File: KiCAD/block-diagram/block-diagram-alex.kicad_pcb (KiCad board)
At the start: 2 copper layers, 12 parts, among them Q3 NMOS, Q4 NMOS, U1 74LS02, U2 74LS02, U3 74LS11, U6 LMC555xM

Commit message: trying to fix issues
Issues with merging are preventing me to pull origin
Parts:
- removed U2: 74LS02, Package_SO:SOIC-14_3.9x8.7mm_P1.27mm
- moved U3 104.8 mm to (151.8, 90.4)
- moved R1 103.7 mm to (156.0, 97.1)
- moved Q4 102.6 mm to (158.5, 92.2)
- moved R3 101.8 mm to (156.0, 103.7)
- moved R4 100.4 mm to (156.0, 107.0)
- moved C3 96.4 mm to (150.4, 97.2)
- moved Q3 95.3 mm to (158.5, 87.5)
- moved R2 95.2 mm to (156.0, 100.4)
- moved U6 91.5 mm to (143.4, 98.8)
- moved C4 86.4 mm to (150.4, 100.5)
- moved U1 63.3 mm to (143.4, 90.4)
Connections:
- U1 pad 10: unconnected-(U1-Pad10) -> Net-(U1-Pad10)
- U1 pad 8: unconnected-(U1-Pad8) -> Net-(R3-Pad2)
- U1 pad 9: unconnected-(U1-Pad9) -> Net-(SW4-B)
- U3 pad 13: Net-(U2-Pad1) -> Net-(U1-Pad10)

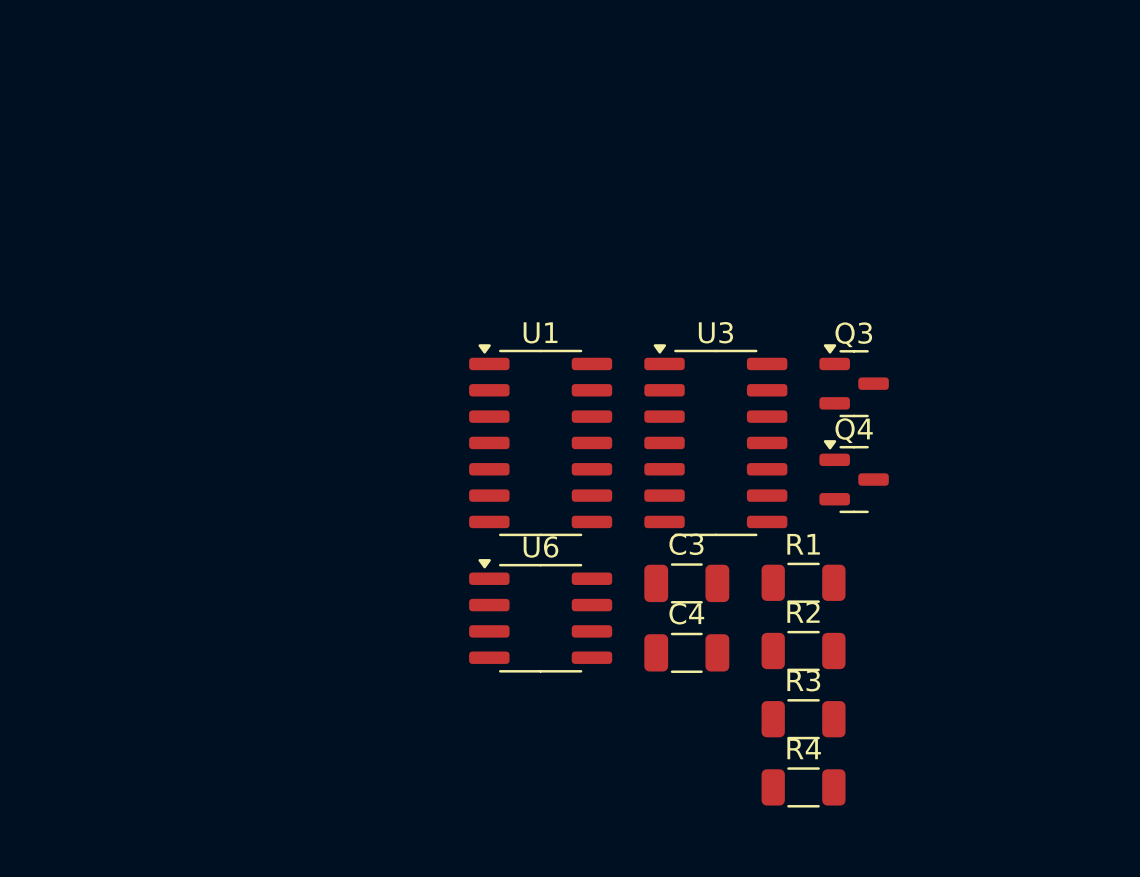
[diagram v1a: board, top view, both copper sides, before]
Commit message: PCB layout updates
I updated the PCB with the components added to the schematic. I dimensioned a rectangle around the board that is 2x1.5 in and placed the 8 pin connecters with respect to the corners of the rectangle. I added the relevant dimensions. Board layout based on our discussion Friday. I remember we were having some discussion on the 4 connectors in each corner of the board, those have not been added yet.
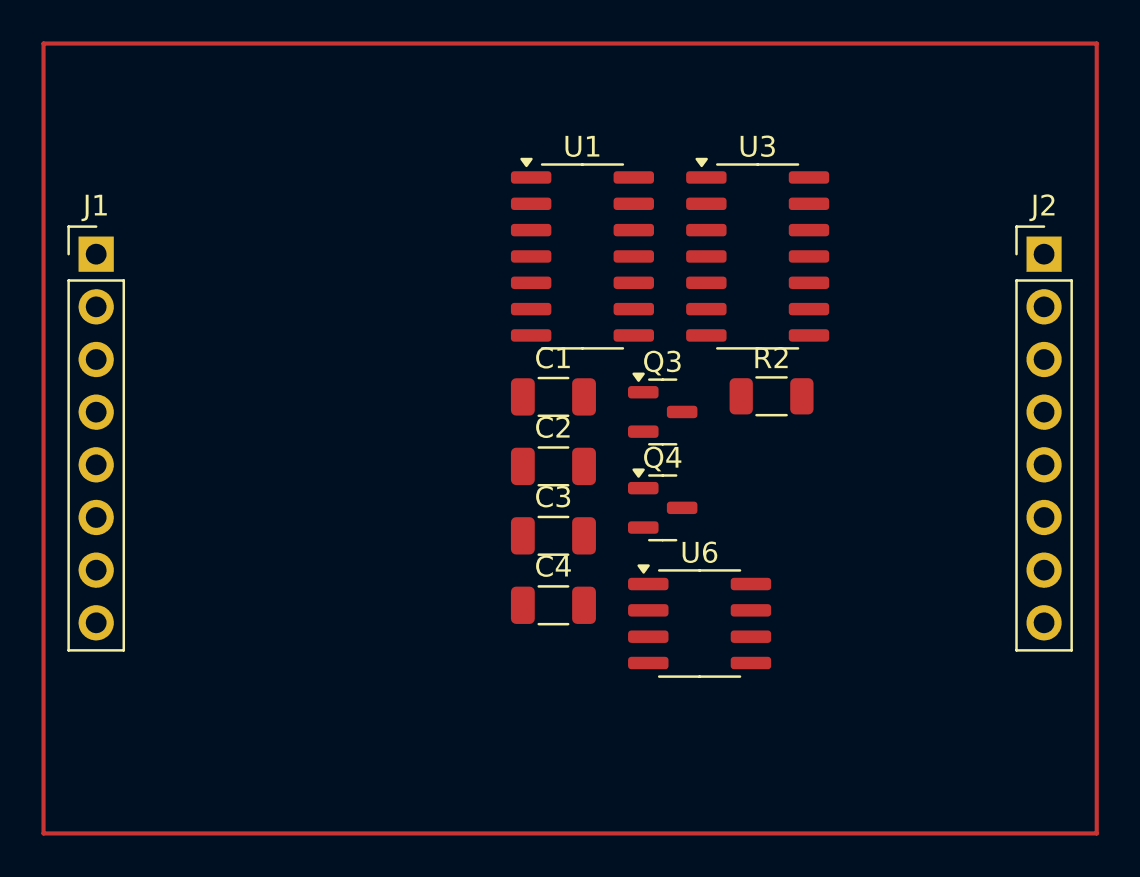
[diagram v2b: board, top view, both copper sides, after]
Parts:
- removed R1, R3, R4: R_US, Resistor_SMD:R_1206_3216Metric
- added C1: C_Small, Capacitor_SMD:C_1206_3216Metric, F.Cu at (144.0, 88.2)
- added C2: C_Small, Capacitor_SMD:C_1206_3216Metric, F.Cu at (144.0, 91.5)
- added J1: Conn_01x08, Connector_PinHeader_2.54mm:PinHeader_1x08_P2.54mm_Vertical, F.Cu at (121.9, 81.3)
- added J2: Conn_01x08, Connector_PinHeader_2.54mm:PinHeader_1x08_P2.54mm_Vertical, F.Cu at (167.6, 81.3)
- moved R2 12.4 mm to (154.5, 88.1)
- moved Q3 9.33 mm to (149.2, 88.9)
- moved Q4 9.33 mm to (149.2, 93.5)
- moved U1 9.22 mm to (145.4, 81.4)
- moved U3 9.22 mm to (153.8, 81.4)
- moved U6 7.67 mm to (151.0, 99.1)
- moved C3 6.83 mm to (144.0, 94.9)
- moved C4 6.83 mm to (144.0, 98.2)
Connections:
- Q4 pad 2: Watchdog_PD_output -> Net-(J1-Pin_3)
- U1 pad 11: unconnected-(U1-Pad11) -> GND
- U1 pad 12: unconnected-(U1-Pad12) -> GND
- U1 pad 14: unconnected-(U1E-VCC-Pad14) -> +5V
- U1 pad 3: Laser_current_high -> Net-(J1-Pin_2)
- U1 pad 7: unconnected-(U1E-GND-Pad7) -> GND
- U3 pad 10: unconnected-(U3-Pad10) -> GND
- U3 pad 11: unconnected-(U3-Pad11) -> GND
- U3 pad 12: LASER_ENA -> Net-(J2-Pin_1)
- U3 pad 14: unconnected-(U3D-VCC-Pad14) -> +5V
- U3 pad 2: Enable_In -> Net-(J1-Pin_4)
- U3 pad 3: unconnected-(U3-Pad3) -> GND
- U3 pad 4: unconnected-(U3-Pad4) -> GND
- U3 pad 5: unconnected-(U3-Pad5) -> GND
- U3 pad 7: unconnected-(U3D-GND-Pad7) -> GND
- U3 pad 9: unconnected-(U3-Pad9) -> GND
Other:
- copper layers 2 -> 4

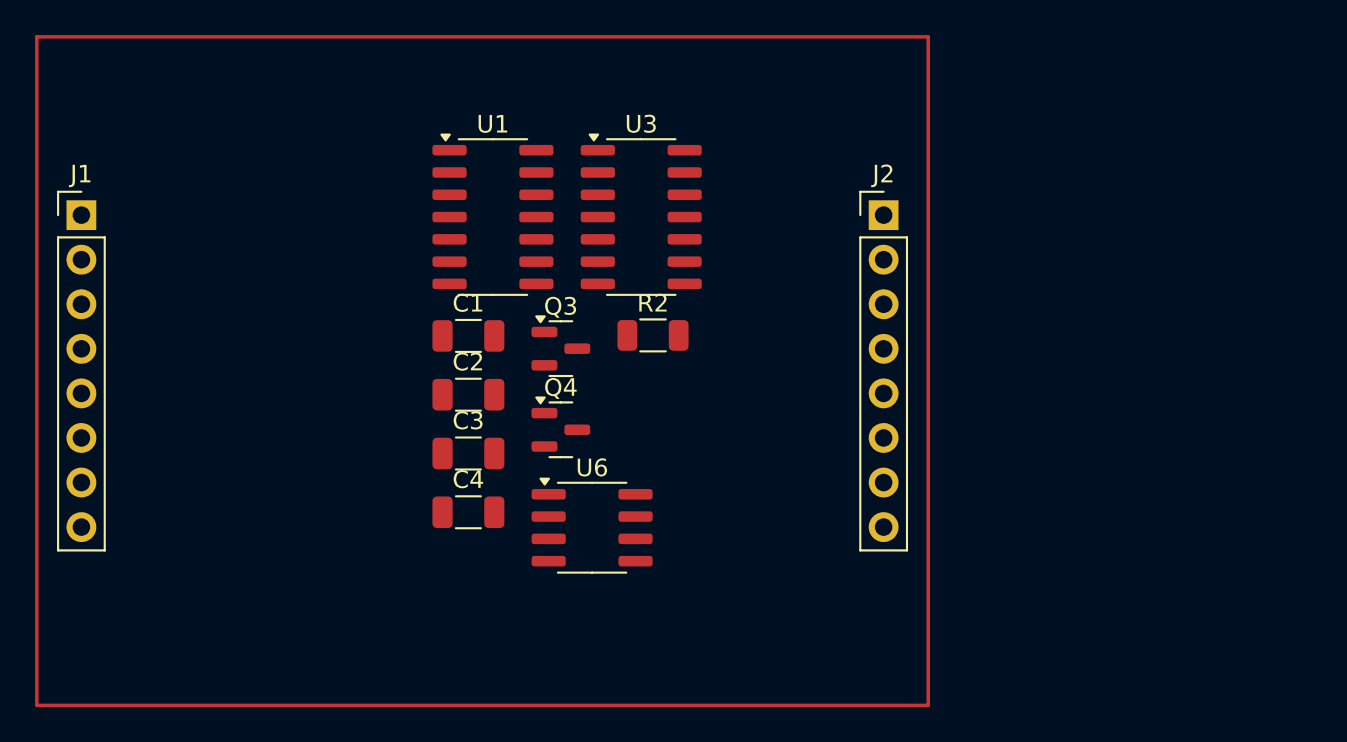
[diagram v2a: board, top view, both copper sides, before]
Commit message: tentative placement, add test points and LEDs
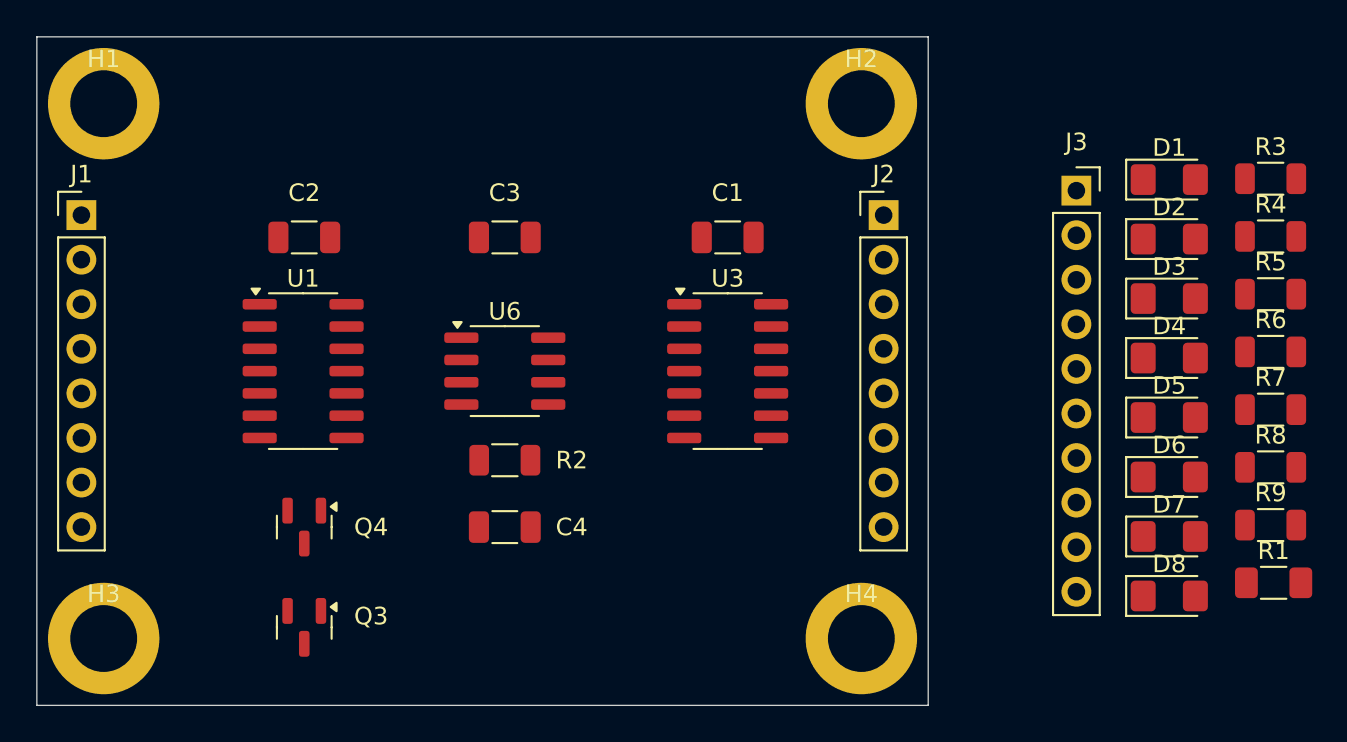
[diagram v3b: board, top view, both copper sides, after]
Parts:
- added D1: LED, LED_SMD:LED_1206_3216Metric_Pad1.42x1.75mm_HandSolder, F.Cu at (183.9, 79.3)
- added D2: LED, LED_SMD:LED_1206_3216Metric_Pad1.42x1.75mm_HandSolder, F.Cu at (183.9, 82.6)
- added D3: LED, LED_SMD:LED_1206_3216Metric_Pad1.42x1.75mm_HandSolder, F.Cu at (183.9, 86.0)
- added D4: LED, LED_SMD:LED_1206_3216Metric_Pad1.42x1.75mm_HandSolder, F.Cu at (183.9, 89.4)
- added D5: LED, LED_SMD:LED_1206_3216Metric_Pad1.42x1.75mm_HandSolder, F.Cu at (183.9, 92.8)
- added D6: LED, LED_SMD:LED_1206_3216Metric_Pad1.42x1.75mm_HandSolder, F.Cu at (183.9, 96.2)
- added D7: LED, LED_SMD:LED_1206_3216Metric_Pad1.42x1.75mm_HandSolder, F.Cu at (183.9, 99.6)
- added D8: LED, LED_SMD:LED_1206_3216Metric_Pad1.42x1.75mm_HandSolder, F.Cu at (183.9, 103.0)
- added H1: MountingHole_Pad, my_mtg_hole:hole_250_150, F.Cu at (123.2, 74.9)
- added H2: MountingHole_Pad, my_mtg_hole:hole_250_150, F.Cu at (166.4, 74.9)
- added H3: MountingHole_Pad, my_mtg_hole:hole_250_150, F.Cu at (123.2, 105.4)
- added H4: MountingHole_Pad, my_mtg_hole:hole_250_150, F.Cu at (166.4, 105.4)
- added J3: Conn_01x10, Connector_PinSocket_2.54mm:PinSocket_1x10_P2.54mm_Vertical, F.Cu at (178.6, 79.9)
- added R1: 470, Resistor_SMD:R_1206_3216Metric_Pad1.30x1.75mm_HandSolder, F.Cu at (189.9, 102.2)
- added R3: 470, Resistor_SMD:R_1206_3216Metric, F.Cu at (189.7, 79.2)
- added R4: 470, Resistor_SMD:R_1206_3216Metric, F.Cu at (189.7, 82.5)
- added R5: 470, Resistor_SMD:R_1206_3216Metric, F.Cu at (189.7, 85.8)
- added R6: 470, Resistor_SMD:R_1206_3216Metric, F.Cu at (189.7, 89.1)
- added R7: 470, Resistor_SMD:R_1206_3216Metric, F.Cu at (189.7, 92.4)
- added R8: 470, Resistor_SMD:R_1206_3216Metric, F.Cu at (189.7, 95.7)
- added R9: 470, Resistor_SMD:R_1206_3216Metric, F.Cu at (189.7, 98.9)
- moved Q3 21.6 mm to (134.6, 104.8), turned to -90 degrees
- moved C1 15.8 mm to (158.8, 82.5), turned to 180 degrees
- moved Q4 15.6 mm to (134.6, 99.1), turned to -90 degrees
- moved U1 13.9 mm to (134.6, 90.2)
- moved C2 13.0 mm to (134.6, 82.5), turned to 180 degrees
- moved C3 12.5 mm to (146.1, 82.5), turned to 180 degrees
- moved R2 11.0 mm to (146.1, 95.2)
- moved U6 10.2 mm to (146.1, 90.2)
- moved U3 10.1 mm to (158.8, 90.2)
- moved C4 2.24 mm to (146.1, 99.1), turned to 180 degrees
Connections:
- net Net-(J1-Pin_1) renamed /OVERRIDE
- net Net-(J1-Pin_2) renamed /LC_HIGH
- net Net-(J1-Pin_3) renamed /WD_PHOTODIODE
- net Net-(J1-Pin_4) renamed /MCU_ENA
- net Net-(J1-Pin_5) renamed /INTERLOCK
- net Net-(J1-Pin_6) renamed /KEY_SW
- net Net-(J2-Pin_1) renamed /LASER_ENA
- net Net-(U6-Q) renamed /WDT_OUT
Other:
- board outline added: 50.8 x 38.1 mm

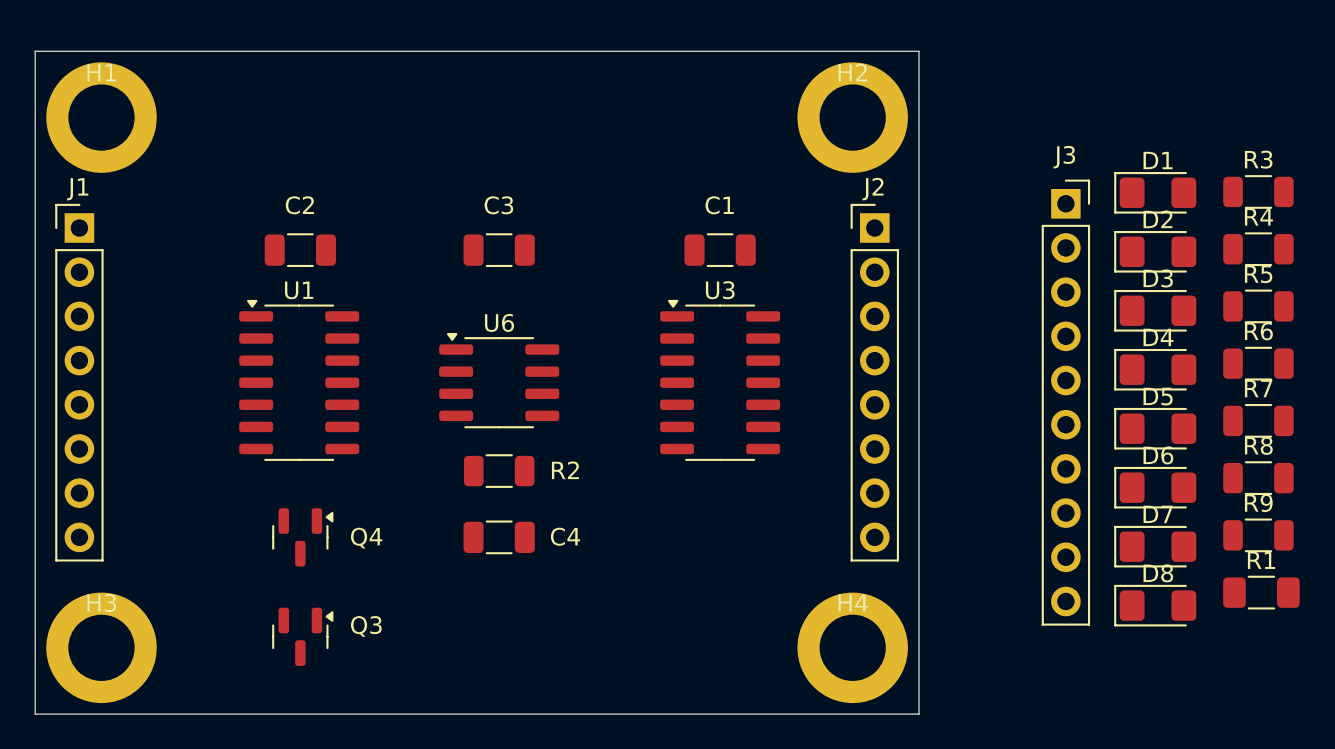
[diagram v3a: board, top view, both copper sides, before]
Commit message: add LEDs and test connector, update placement
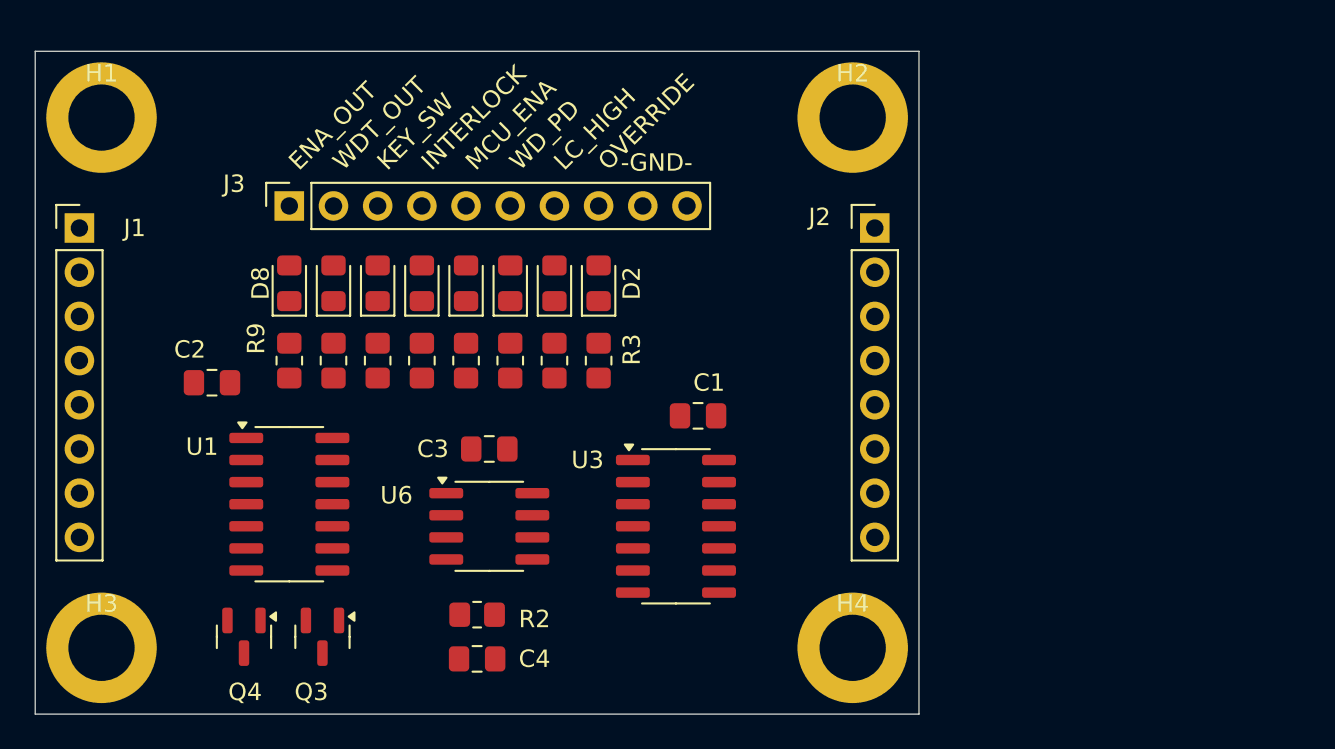
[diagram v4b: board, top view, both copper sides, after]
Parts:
- C1, C2, C3, C4: footprint Capacitor_SMD:C_1206_3216Metric -> Capacitor_SMD:C_0805_2012Metric_Pad1.18x1.45mm_HandSolder
- D1, D2, D3, D4, D5, D6, D7, D8: footprint LED_SMD:LED_1206_3216Metric_Pad1.42x1.75mm_HandSolder -> LED_SMD:LED_0805_2012Metric_Pad1.15x1.40mm_HandSolder
- R1: footprint Resistor_SMD:R_1206_3216Metric_Pad1.30x1.75mm_HandSolder -> Resistor_SMD:R_0805_2012Metric_Pad1.20x1.40mm_HandSolder
- R2, R3, R4, R5, R6, R7, R8, R9: footprint Resistor_SMD:R_1206_3216Metric -> Resistor_SMD:R_0805_2012Metric_Pad1.20x1.40mm_HandSolder
- moved R9 56.6 mm to (134.0, 88.9), turned to 90 degrees
- moved R8 53.6 mm to (136.5, 88.9), turned to 90 degrees
- moved D8 53.3 mm to (134.0, 84.5), turned to 90 degrees
- moved R7 50.7 mm to (139.1, 88.9), turned to 90 degrees
- moved D7 49.8 mm to (136.5, 84.5), turned to 90 degrees
- moved R6 48.1 mm to (141.6, 88.9), turned to -90 degrees
- moved D6 46.4 mm to (139.1, 84.5), turned to 90 degrees
- moved R5 45.7 mm to (144.1, 88.9), turned to -90 degrees
- moved J3 44.6 mm to (134.0, 80.0), turned to 90 degrees
- moved R4 43.5 mm to (146.7, 88.9), turned to -90 degrees
- moved D5 43.1 mm to (141.6, 84.5), turned to 90 degrees
- moved R1 42.8 mm to (149.2, 88.9), turned to -90 degrees
- moved D4 40.1 mm to (144.1, 84.5), turned to 90 degrees
- moved R3 39.1 mm to (151.8, 88.9), turned to -90 degrees
- moved D3 37.3 mm to (146.7, 84.5), turned to 90 degrees
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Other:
- board text added: "-GND-"
- board text added: "ENA_OUT"
- board text added: "INTERLOCK"
- board text added: "KEY_SW"
- board text added: "LC_HIGH"
- board text added: "MCU_ENA"
- board text added: "OVERRIDE"
- board text added: "WDT_OUT"
- board text added: "WD_PD"

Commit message: tweak placement
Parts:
- turned D1 to -90 degrees
- turned D2 to -90 degrees
- turned D3 to -90 degrees
- turned D4 to -90 degrees
- turned D5 to -90 degrees
- turned D6 to -90 degrees
- turned D7 to -90 degrees
- turned D8 to -90 degrees

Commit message: fix some connectors
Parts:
- J1, J2: moved to B.Cu
- J3: footprint Connector_PinSocket_2.54mm:PinSocket_1x10_P2.54mm_Vertical -> Connector_PinHeader_2.54mm:PinHeader_1x10_P2.54mm_Vertical
- turned J1 to 180 degrees
- turned J2 to 180 degrees

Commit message: demo some routing
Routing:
- net /KEY_SW: track 0.00 -> 27.6 mm, vias 0 -> 1
- net /OVERRIDE: track 0.00 -> 26.0 mm, vias 0 -> 2
- net /LC_HIGH: track 0.00 -> 24.0 mm, vias 0 -> 2
- net /INTERLOCK: track 0.00 -> 22.2 mm, vias 0 -> 2
- net GND: track 0.00 -> 21.2 mm, vias 0 -> 6
- net /WDT_OUT: track 0.00 -> 10.7 mm
- net /LASER_ENA: track 0.00 -> 10.7 mm
- net +5V: track 0.00 -> 2.87 mm, vias 0 -> 2
- added copper zone on In2.Cu, net +5V
- added copper zone on In1.Cu, net GND
